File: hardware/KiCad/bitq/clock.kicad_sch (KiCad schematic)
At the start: 1 part, among them U1 ICM7555xB

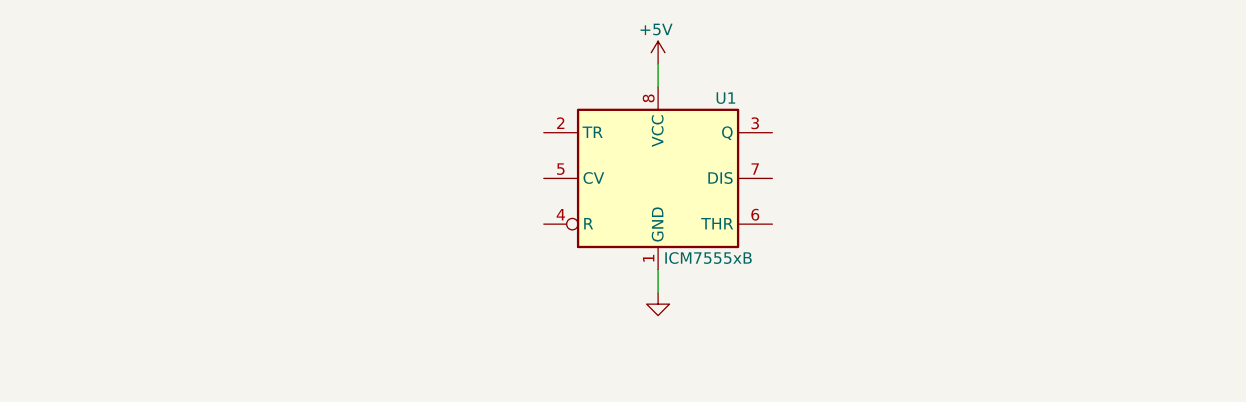
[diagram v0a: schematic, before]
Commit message: feat: hardware: Adds two more 555 timer instance for monostable and bistable timers
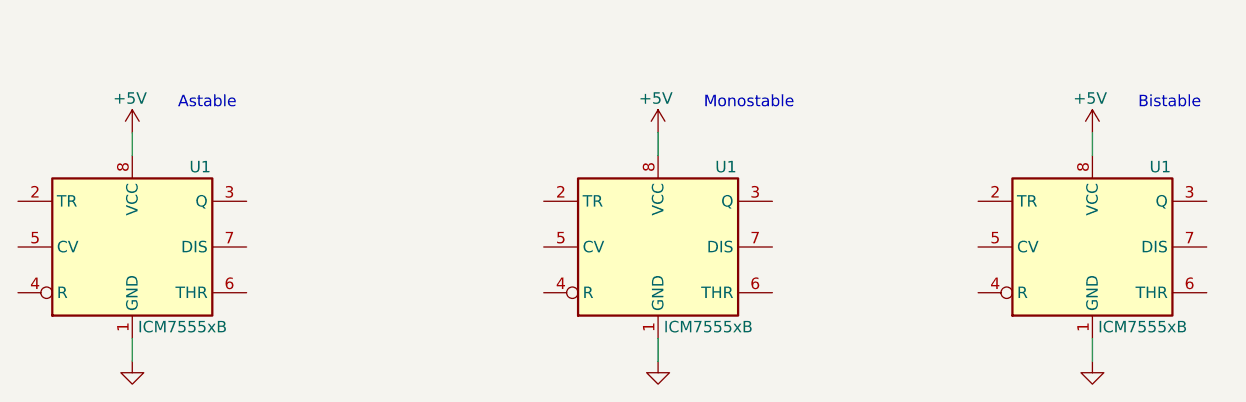
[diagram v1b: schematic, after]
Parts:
- added U1 (x2): ICM7555xB, Package_SO:SOIC-8_3.9x4.9mm_P1.27mm, symbol Timer:ICM7555xB
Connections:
- net +5V: now also U1.8 (VCC), U1.8 (VCC)
- net GND: now also U1.1 (GND), U1.1 (GND)
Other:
- note added: "Astable"
- note added: "Bistable"
- note added: "Monostable"
- moved on the sheet: U1
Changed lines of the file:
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@@
 (kicad_sch (version 20230121) (generator eeschema)
   (paper "A4")
-  (wire (pts (xy 147.32 68.58) (xy 147.32 71.12))
-    (stroke (width 0) (type default))
-  )
-  (wire (pts (xy 147.32 91.44) (xy 147.32 93.98))
-    (stroke (width 0) (type default))
-  )
-  (symbol (lib_id "Timer:ICM7555xB") (at 147.32 81.28 0) (unit 1)
-    (in_bom yes) (on_board yes) (dnp no)
-    (property "Reference" "U1" (at 153.67 72.39 0)
-      (effects (font (size 1.27 1.27)) (justify left))
-    )
-    (property "Value" "ICM7555xB" (at 147.955 90.17 0)
-      (effects (font (size 1.27 1.27)) (justify left))
-    )
-    (property "Footprint" "Package_SO:SOIC-8_3.9x4.9mm_P1.27mm" (at 168.91 91.44 0)
-      (effects (font (size 1.27 1.27)) hide)
-    )
-    (property "Datasheet" "http://www.intersil.com/content/dam/Intersil/documents/icm7/icm7555-56.pdf" (at 168.91 91.44 0)
+  (wire (pts (xy 88.9 76.2) (xy 88.9 78.74))
+    (stroke (width 0) (type default))
+  )
+  (wire (pts (xy 195.58 76.2) (xy 195.58 78.74))
+    (stroke (width 0) (type default))
+  )
+  (wire (pts (xy 147.32 76.2) (xy 147.32 78.74))
+    (stroke (width 0) (type default))
+  )
+  (wire (pts (xy 88.9 99.06) (xy 88.9 101.6))
+    (stroke (width 0) (type default))
+  )
+  (wire (pts (xy 195.58 99.06) (xy 195.58 101.6))
+    (stroke (width 0) (type default))
+  )
+  (wire (pts (xy 147.32 99.06) (xy 147.32 101.6))
+    (stroke (width 0) (type default))
+  )
+  (text "Monostable" (at 152.4 73.66 0)
+    (effects (font (size 1.27 1.27)) (justify left bottom))
+  )
+  (text "Astable" (at 93.98 73.66 0)
+    (effects (font (size 1.27 1.27)) (justify left bottom))
+  )
+  (text "Bistable" (at 200.66 73.66 0)
+    (effects (font (size 1.27 1.27)) (justify left bottom))
+  )
+  (symbol (lib_id "power:GND") (at 147.32 101.6 0) (unit 1)
+    (in_bom yes) (on_board yes) (dnp no) (fields_autoplaced)
+    (property "Reference" "#PWR04" (at 147.32 107.95 0)
+      (effects (font (size 1.27 1.27)) hide)
+    )
+    (property "Value" "GND" (at 147.32 106.68 0)
+      (effects (font (size 1.27 1.27)) hide)
+    )
+    (property "Footprint" "" (at 147.32 101.6 0)
+      (effects (font (size 1.27 1.27)) hide)
+    )
+    (property "Datasheet" "" (at 147.32 101.6 0)
+      (effects (font (size 1.27 1.27)) hide)
+    )
+    (pin "1")
+    (instances
+      (project "bitq"
+        (path "/b036fac6-0b73-4a9f-b939-38afaf28d9b2/7dd0c87e-f912-47d8-bbb7-1c32d501dad7"
+          (reference "#PWR04") (unit 1)
+        )
+      )
+    )
+  )
+  (symbol (lib_id "Timer:ICM7555xB") (at 147.32 88.9 0) (unit 1)
+    (in_bom yes) (on_board yes) (dnp no)
+    (property "Reference" "U1" (at 153.67 80.01 0)
+      (effects (font (size 1.27 1.27)) (justify left))
+    )
+    (property "Value" "ICM7555xB" (at 147.955 97.79 0)
+      (effects (font (size 1.27 1.27)) (justify left))
+    )
+    (property "Footprint" "Package_SO:SOIC-8_3.9x4.9mm_P1.27mm" (at 168.91 99.06 0)
+      (effects (font (size 1.27 1.27)) hide)
+    )
+    (property "Datasheet" "http://www.intersil.com/content/dam/Intersil/documents/icm7/icm7555-56.pdf" (at 168.91 99.06 0)
       (effects (font (size 1.27 1.27)) hide)
     )
@@
         )
         (path "/b036fac6-0b73-4a9f-b939-38afaf28d9b2/7dd0c87e-f912-47d8-bbb7-1c32d501dad7"
-          (reference "U1") (unit 1)
-        )
-      )
-    )
-  )
-  (symbol (lib_id "power:+5V") (at 147.32 68.58 0) (unit 1)
-    (in_bom yes) (on_board yes) (dnp no)
-    (property "Reference" "#PWR02" (at 147.32 72.39 0)
-      (effects (font (size 1.27 1.27)) hide)
-    )
-    (property "Value" "+5V" (at 147.066 64.77 0)
+          (reference "U2") (unit 1)
+        )
+      )
+    )
+  )
+  (symbol (lib_id "power:+5V") (at 195.58 76.2 0) (unit 1)
+    (in_bom yes) (on_board yes) (dnp no)
+    (property "Reference" "#PWR05" (at 195.58 80.01 0)
+      (effects (font (size 1.27 1.27)) hide)
+    )
+    (property "Value" "+5V" (at 195.326 72.39 0)
       (effects (font (size 1.27 1.27)))
     )
-    (property "Footprint" "" (at 147.32 68.58 0)
-      (effects (font (size 1.27 1.27)) hide)
-    )
-    (property "Datasheet" "" (at 147.32 68.58 0)
+    (property "Footprint" "" (at 195.58 76.2 0)
+      (effects (font (size 1.27 1.27)) hide)
+    )
+    (property "Datasheet" "" (at 195.58 76.2 0)
+      (effects (font (size 1.27 1.27)) hide)
+    )
+    (pin "1")
+    (instances
+      (project "bitq"
+        (path "/b036fac6-0b73-4a9f-b939-38afaf28d9b2/7dd0c87e-f912-47d8-bbb7-1c32d501dad7"
+          (reference "#PWR05") (unit 1)
+        )
+      )
+    )
+  )
+  (symbol (lib_id "Timer:ICM7555xB") (at 88.9 88.9 0) (unit 1)
+    (in_bom yes) (on_board yes) (dnp no)
+    (property "Reference" "U1" (at 95.25 80.01 0)
+      (effects (font (size 1.27 1.27)) (justify left))
+    )
+    (property "Value" "ICM7555xB" (at 89.535 97.79 0)
+      (effects (font (size 1.27 1.27)) (justify left))
+    )
+    (property "Footprint" "Package_SO:SOIC-8_3.9x4.9mm_P1.27mm" (at 110.49 99.06 0)
+      (effects (font (size 1.27 1.27)) hide)
+    )
+    (property "Datasheet" "http://www.intersil.com/content/dam/Intersil/documents/icm7/icm7555-56.pdf" (at 110.49 99.06 0)
+      (effects (font (size 1.27 1.27)) hide)
+    )
+    (pin "1")
+    (pin "8")
+    (pin "2")
+    (pin "3")
+    (pin "4")
+    (pin "5")
+    (pin "6")
+    (pin "7")
+    (instances
+      (project "bitq"
+        (path "/b036fac6-0b73-4a9f-b939-38afaf28d9b2"
+          (reference "U1") (unit 1)
+        )
+        (path "/b036fac6-0b73-4a9f-b939-38afaf28d9b2/7dd0c87e-f912-47d8-bbb7-1c32d501dad7"
+          (reference "U1") (unit 1)
+        )
+      )
+    )
+  )
+  (symbol (lib_id "power:+5V") (at 88.9 76.2 0) (unit 1)
+    (in_bom yes) (on_board yes) (dnp no)
+    (property "Reference" "#PWR02" (at 88.9 80.01 0)
+      (effects (font (size 1.27 1.27)) hide)
+    )
+    (property "Value" "+5V" (at 88.646 72.39 0)
+      (effects (font (size 1.27 1.27)))
+    )
+    (property "Footprint" "" (at 88.9 76.2 0)
+      (effects (font (size 1.27 1.27)) hide)
+    )
+    (property "Datasheet" "" (at 88.9 76.2 0)
       (effects (font (size 1.27 1.27)) hide)
     )
@@
     )
   )
-  (symbol (lib_id "power:GND") (at 147.32 93.98 0) (unit 1)
+  (symbol (lib_id "power:GND") (at 195.58 101.6 0) (unit 1)
     (in_bom yes) (on_board yes) (dnp no) (fields_autoplaced)
-    (property "Reference" "#PWR01" (at 147.32 100.33 0)
-      (effects (font (size 1.27 1.27)) hide)
-    )
-    (property "Value" "GND" (at 147.32 99.06 0)
-      (effects (font (size 1.27 1.27)) hide)
-    )
-    (property "Footprint" "" (at 147.32 93.98 0)
-      (effects (font (size 1.27 1.27)) hide)
-    )
-    (property "Datasheet" "" (at 147.32 93.98 0)
+    (property "Reference" "#PWR06" (at 195.58 107.95 0)
+      (effects (font (size 1.27 1.27)) hide)
+    )
+    (property "Value" "GND" (at 195.58 106.68 0)
+      (effects (font (size 1.27 1.27)) hide)
+    )
+    (property "Footprint" "" (at 195.58 101.6 0)
+      (effects (font (size 1.27 1.27)) hide)
+    )
+    (property "Datasheet" "" (at 195.58 101.6 0)
+      (effects (font (size 1.27 1.27)) hide)
+    )
+    (pin "1")
+    (instances
+      (project "bitq"
+        (path "/b036fac6-0b73-4a9f-b939-38afaf28d9b2/7dd0c87e-f912-47d8-bbb7-1c32d501dad7"
+          (reference "#PWR06") (unit 1)
+        )
+      )
+    )
+  )
+  (symbol (lib_id "power:GND") (at 88.9 101.6 0) (unit 1)
+    (in_bom yes) (on_board yes) (dnp no) (fields_autoplaced)
+    (property "Reference" "#PWR01" (at 88.9 107.95 0)
+      (effects (font (size 1.27 1.27)) hide)
+    )
+    (property "Value" "GND" (at 88.9 106.68 0)
+      (effects (font (size 1.27 1.27)) hide)
+    )
+    (property "Footprint" "" (at 88.9 101.6 0)
+      (effects (font (size 1.27 1.27)) hide)
+    )
+    (property "Datasheet" "" (at 88.9 101.6 0)
       (effects (font (size 1.27 1.27)) hide)
     )
@@
         )
       )
+    )
+  )
+  (symbol (lib_id "power:+5V") (at 147.32 76.2 0) (unit 1)
+    (in_bom yes) (on_board yes) (dnp no)
+    (property "Reference" "#PWR03" (at 147.32 80.01 0)
+      (effects (font (size 1.27 1.27)) hide)
+    )
+    (property "Value" "+5V" (at 147.066 72.39 0)
+      (effects (font (size 1.27 1.27)))
+    )
+    (property "Footprint" "" (at 147.32 76.2 0)
+      (effects (font (size 1.27 1.27)) hide)
+    )
+    (property "Datasheet" "" (at 147.32 76.2 0)
+      (effects (font (size 1.27 1.27)) hide)
+    )
+    (pin "1")
+    (instances
+      (project "bitq"
+        (path "/b036fac6-0b73-4a9f-b939-38afaf28d9b2/7dd0c87e-f912-47d8-bbb7-1c32d501dad7"
+          (reference "#PWR03") (unit 1)
+        )
+      )
+    )
+  )
+  (symbol (lib_id "Timer:ICM7555xB") (at 195.58 88.9 0) (unit 1)
+    (in_bom yes) (on_board yes) (dnp no)
+    (property "Reference" "U1" (at 201.93 80.01 0)
+      (effects (font (size 1.27 1.27)) (justify left))
+    )
+    (property "Value" "ICM7555xB" (at 196.215 97.79 0)
+      (effects (font (size 1.27 1.27)) (justify left))
+    )
+    (property "Footprint" "Package_SO:SOIC-8_3.9x4.9mm_P1.27mm" (at 217.17 99.06 0)
+      (effects (font (size 1.27 1.27)) hide)
+    )
+    (property "Datasheet" "http://www.intersil.com/content/dam/Intersil/documents/icm7/icm7555-56.pdf" (at 217.17 99.06 0)
+      (effects (font (size 1.27 1.27)) hide)
+    )
+    (pin "1")
+    (pin "8")
+    (pin "2")
+    (pin "3")
+    (pin "4")
+    (pin "5")
+    (pin "6")
+    (pin "7")
+    (instances
+      (project "bitq"
+        (path "/b036fac6-0b73-4a9f-b939-38afaf28d9b2"
+          (reference "U1") (unit 1)
+        )
+        (path "/b036fac6-0b73-4a9f-b939-38afaf28d9b2/7dd0c87e-f912-47d8-bbb7-1c32d501dad7"
+          (reference "U3") (unit 1)
+        )
+      )
